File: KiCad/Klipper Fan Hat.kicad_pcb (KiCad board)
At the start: 2 copper layers, 65 x 56 mm, 62 parts, among them J1 Vin, J2 Serial, J3 I2C, J4 1 Wire, J5 GPIO5, J6 GPIO6, J7 SPI, J8 GPIO, Q1 IRLML6344, Q2 IRLML6344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

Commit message: update values of pull up resistors
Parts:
- R4, R5, R6: value 3.9k -> 4.7k

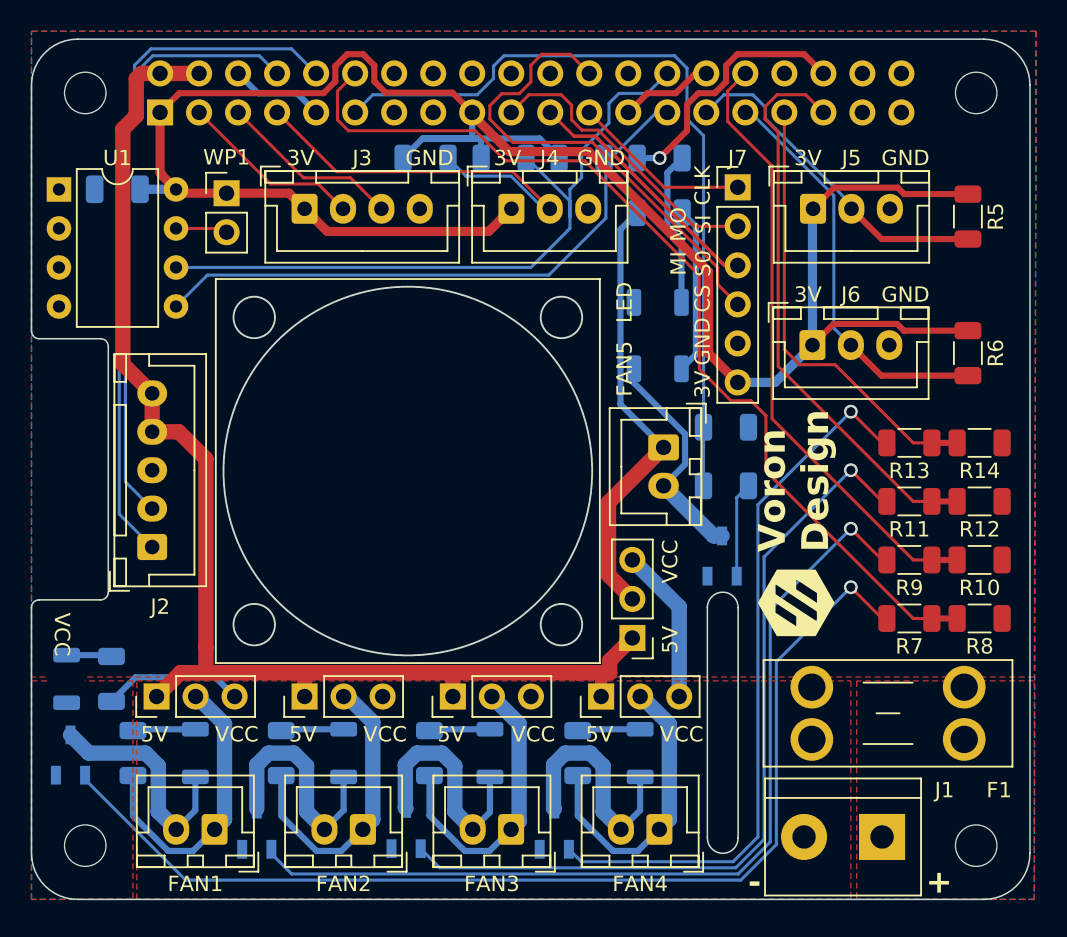
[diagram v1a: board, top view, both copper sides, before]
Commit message: Update KlippUpdate Klipper Fan Hat to expose more GPIO pins and add an on board DS18B20 Temperature Sensor
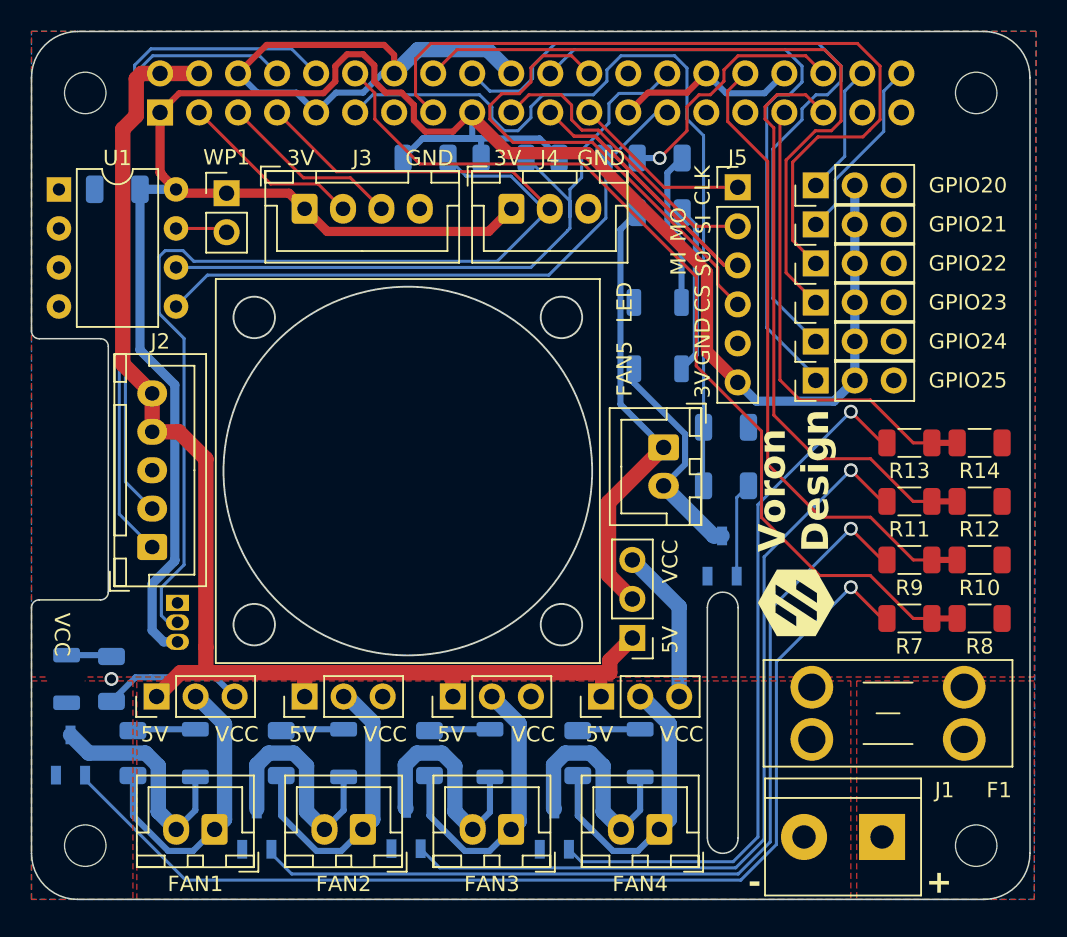
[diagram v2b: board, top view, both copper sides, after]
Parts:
- removed the J5 at (150.9, 55.0)
- removed R5, R6: 4.7k, Resistor_SMD:R_1206_3216Metric
- added GPIO20: J7, Connector_PinHeader_2.54mm:PinHeader_1x03_P2.54mm_Vertical, F.Cu at (151.1, 53.5)
- added GPIO21: J8, Connector_PinHeader_2.54mm:PinHeader_1x03_P2.54mm_Vertical, F.Cu at (151.1, 56.1)
- added GPIO22: J9, Connector_PinHeader_2.54mm:PinHeader_1x03_P2.54mm_Vertical, F.Cu at (151.1, 58.6)
- added GPIO24: J11, Connector_PinHeader_2.54mm:PinHeader_1x03_P2.54mm_Vertical, F.Cu at (151.1, 63.7)
- added GPIO25: J12, Connector_PinHeader_2.54mm:PinHeader_1x03_P2.54mm_Vertical, F.Cu at (151.1, 66.2)
- added U2: DS18B20, Package_TO_SOT_THT:TO-92_Inline, B.Cu at (109.5, 80.7)
- GPIO23: renamed from J6; value GPIO6 -> J10; footprint Connector_JST:JST_XH_B3B-XH-A_1x03_P2.50mm_Vertical -> Connector_PinHeader_2.54mm:PinHeader_1x03_P2.54mm_Vertical
- moved GPIO23 2.79 mm to (151.1, 61.1), turned to 90 degrees
- renumbered J7 to J5, J8 to J6
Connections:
- GPIO23 pad 1: +3V3 -> /GPIO23
- GPIO23 pad 2: /GPIO6 -> +3V3
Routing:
- net /GPIO4/GPCLK0: track 28.3 -> 81.5 mm
- net /GPIO22: track 0.00 -> 52.8 mm
- net /GPIO24: track 0.00 -> 48.2 mm
- net /GPIO23: track 0.00 -> 45.9 mm
- net /GPIO25: track 0.00 -> 40.7 mm
- net GND: track 12.3 -> 45.9 mm, vias 0 -> 1
- net /GPIO6: track 26.6 -> 0.00 mm
- net /GPIO5: track 22.0 -> 0.00 mm
- net +3V3: track 138.2 -> 157.1 mm
- net /GPIO21/PCM.DOUT: track 0.00 -> 12.1 mm
- net /GPIO20/PCM.DIN: track 0.00 -> 8.55 mm
- net /GPIO17: track 51.6 -> 54.3 mm
- net /GPIO19/PCM.FS: track 37.1 -> 39.2 mm
- net /GPIO12/PWM0: track 40.0 -> 41.9 mm
- net /GPIO13/PWM1: track 29.2 -> 30.8 mm
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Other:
- board size 65 x 56 mm -> 65 x 56.5 mm
- board text removed: "Extend PCB edge 0.5mm if using SMT header"

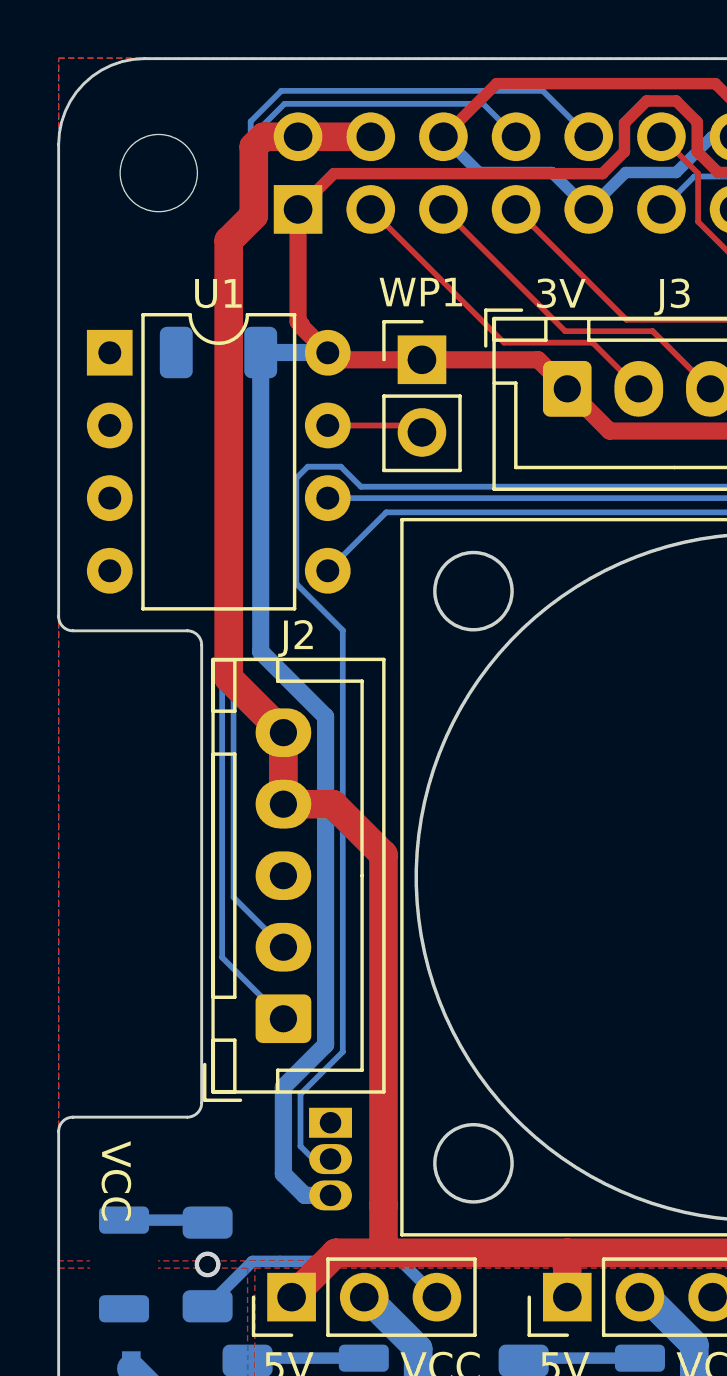
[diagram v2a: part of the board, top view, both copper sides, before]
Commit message: Update Serial Header Ground connection
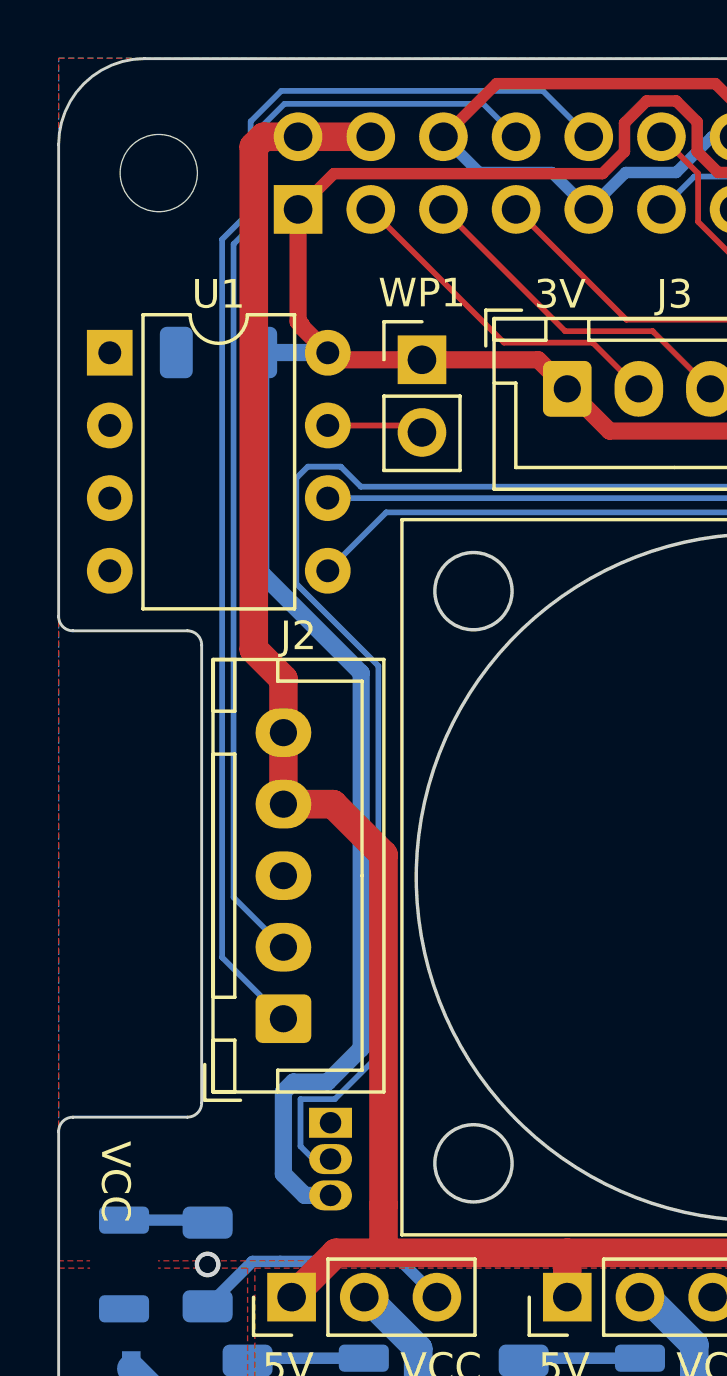
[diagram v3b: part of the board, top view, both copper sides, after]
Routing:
- net +3V3: track 157.1 -> 158.8 mm
- net /GPIO4/GPCLK0: track 81.5 -> 83.3 mm
- net +5V: track 84.2 -> 83.5 mm
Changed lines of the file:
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@@
   (segment (start 119.846 52.626) (end 131.326 52.626) (width 0.2) (layer "F.Cu") (net 4))
   (segment (start 128.2915 52.915) (end 127.1165 51.74) (width 0.2) (layer "B.Cu") (net 4))
+  (segment (start 130.322 58.462) (end 133.742 55.042) (width 0.2) (layer "B.Cu") (net 4))
+  (segment (start 133.742 55.042) (end 133.344817 55.042) (width 0.2) (layer "B.Cu") (net 4))
+  (segment (start 108.454 79.871) (end 109.652 79.871) (width 0.2) (layer "B.Cu") (net 4))
+  (segment (start 131.217817 52.915) (end 128.2915 52.915) (width 0.2) (layer "B.Cu") (net 4))
+  (segment (start 108.308 61.857635) (end 108.308 58.164) (width 0.2) (layer "B.Cu") (net 4))
+  (segment (start 108.308 58.164) (end 108.71 57.762) (width 0.2) (layer "B.Cu") (net 4))
+  (segment (start 110.563635 58.462) (end 130.322 58.462) (width 0.2) (layer "B.Cu") (net 4))
+  (segment (start 111.176 78.347) (end 111.176 64.725636) (width 0.2) (layer "B.Cu") (net 4))
+  (segment (start 108.454 81.521) (end 108.454 79.871) (width 0.2) (layer "B.Cu") (net 4))
   (segment (start 108.71 57.762) (end 109.863635 57.762) (width 0.2) (layer "B.Cu") (net 4))
-  (segment (start 133.742 55.042) (end 133.344817 55.042) (width 0.2) (layer "B.Cu") (net 4))
-  (segment (start 108.454 81.521) (end 108.454 79.697188) (width 0.2) (layer "B.Cu") (net 4))
-  (segment (start 108.308 61.857635) (end 108.308 58.164) (width 0.2) (layer "B.Cu") (net 4))
+  (segment (start 133.344817 55.042) (end 131.217817 52.915) (width 0.2) (layer "B.Cu") (net 4))
+  (segment (start 109.652 79.871) (end 111.176 78.347) (width 0.2) (layer "B.Cu") (net 4))
+  (segment (start 109.504 81.966) (end 108.899 81.966) (width 0.2) (layer "B.Cu") (net 4))
+  (segment (start 111.176 64.725636) (end 108.308 61.857635) (width 0.2) (layer "B.Cu") (net 4))
+  (segment (start 108.899 81.966) (end 108.454 81.521) (width 0.2) (layer "B.Cu") (net 4))
   (segment (start 109.863635 57.762) (end 110.563635 58.462) (width 0.2) (layer "B.Cu") (net 4))
-  (segment (start 108.454 79.697188) (end 109.932 78.219188) (width 0.2) (layer "B.Cu") (net 4))
-  (segment (start 131.217817 52.915) (end 128.2915 52.915) (width 0.2) (layer "B.Cu") (net 4))
-  (segment (start 109.932 63.481635) (end 108.308 61.857635) (width 0.2) (layer "B.Cu") (net 4))
-  (segment (start 110.563635 58.462) (end 130.322 58.462) (width 0.2) (layer "B.Cu") (net 4))
-  (segment (start 108.899 81.966) (end 108.454 81.521) (width 0.2) (layer "B.Cu") (net 4))
-  (segment (start 109.504 81.966) (end 108.899 81.966) (width 0.2) (layer "B.Cu") (net 4))
-  (segment (start 130.322 58.462) (end 133.742 55.042) (width 0.2) (layer "B.Cu") (net 4))
-  (segment (start 133.344817 55.042) (end 131.217817 52.915) (width 0.2) (layer "B.Cu") (net 4))
-  (segment (start 109.932 78.219188) (end 109.932 63.481635) (width 0.2) (layer "B.Cu") (net 4))
-  (segment (start 108.308 58.164) (end 108.71 57.762) (width 0.2) (layer "B.Cu") (net 4))
   (segment (start 107.893654 45.08) (end 114.84 45.08) (width 0.2) (layer "B.Cu") (net 5))
   (segment (start 106.115 49.981686) (end 107.112 48.984686) (width 0.2) (layer "B.Cu") (net 5))
@@
   (segment (start 155.48 50.005654) (end 152.324 53.161654) (width 0.2) (layer "B.Cu") (net 29))
   (segment (start 156.63 46.23) (end 155.48 47.38) (width 0.2) (layer "B.Cu") (net 29))
+  (segment (start 107.167919 46.23) (end 106.82 46.577919) (width 1) (layer "F.Cu") (net 30))
+  (segment (start 108.37 46.23) (end 107.167919 46.23) (width 1) (layer "F.Cu") (net 30))
   (segment (start 111.3538 85.242) (end 117.78 85.242) (width 1) (layer "F.Cu") (net 30))
   (segment (start 111.3538 83.5812) (end 111.3538 85.242) (width 1) (layer "F.Cu") (net 30))
-  (segment (start 107.8524 67.06) (end 105.9436 65.1512) (width 1) (layer "F.Cu") (net 30))
   (segment (start 127.432 85.242) (end 135.534 85.242) (width 1) (layer "F.Cu") (net 30))
-  (segment (start 106.82 48.984) (end 106.82 46.577919) (width 1) (layer "F.Cu") (net 30))
   (segment (start 137.6428 84.4552) (end 139.116 82.982) (width 1) (layer "F.Cu") (net 30))
   (segment (start 137.6428 85.2426) (end 137.6428 84.4552) (width 1) (layer "F.Cu") (net 30))
   (segment (start 107.857 69.56) (end 107.857 67.06) (width 1) (layer "F.Cu") (net 30))
   (segment (start 111.3538 71.3234) (end 111.3538 83.5812) (width 1) (layer "F.Cu") (net 30))
-  (segment (start 107.167919 46.23) (end 108.37 46.23) (width 1) (layer "F.Cu") (net 30))
   (segment (start 109.693 85.242) (end 108.143 86.792) (width 1) (layer "F.Cu") (net 30))
   (segment (start 135.534 85.242) (end 135.5346 85.2426) (width 1) (layer "F.Cu") (net 30))
   (segment (start 107.857 69.56) (end 109.5904 69.56) (width 1) (layer "F.Cu") (net 30))
   (segment (start 111.3538 85.242) (end 109.693 85.242) (width 1) (layer "F.Cu") (net 30))
+  (segment (start 106.82 64.148) (end 107.857 65.185) (width 1) (layer "F.Cu") (net 30))
   (segment (start 135.5346 85.2426) (end 137.084 85.2426) (width 1) (layer "F.Cu") (net 30))
-  (segment (start 105.9436 65.1512) (end 105.9436 49.8604) (width 1) (layer "F.Cu") (net 30))
-  (segment (start 107.857 67.06) (end 107.8524 67.06) (width 1) (layer "F.Cu") (net 30))
-  (segment (start 106.82 46.577919) (end 107.167919 46.23) (width 1) (layer "F.Cu") (net 30))
+  (segment (start 107.857 65.185) (end 107.857 67.06) (width 1) (layer "F.Cu") (net 30))
   (segment (start 127.432 86.792) (end 127.432 85.242) (width 1) (layer "F.Cu") (net 30))
   (segment (start 137.084 86.792) (end 137.084 85.2426) (width 0.8) (layer "F.Cu") (net 30))
+  (segment (start 106.82 46.577919) (end 106.82 64.148) (width 1) (layer "F.Cu") (net 30))
   (segment (start 109.5904 69.56) (end 111.3538 71.3234) (width 1) (layer "F.Cu") (net 30))
   (segment (start 117.78 86.792) (end 117.78 85.242) (width 1) (layer "F.Cu") (net 30))
@@
   (segment (start 137.084 85.2426) (end 137.6428 85.2426) (width 1) (layer "F.Cu") (net 30))
   (segment (start 117.78 85.242) (end 127.432 85.242) (width 1) (layer "F.Cu") (net 30))
-  (segment (start 105.9436 49.8604) (end 106.82 48.984) (width 1) (layer "F.Cu") (net 30))
   (segment (start 128.69 49.052844) (end 128.69 48.77) (width 0.8) (layer "F.Cu") (net 31))
   (segment (start 108.37 52.6932) (end 108.37 48.77) (width 0.6) (layer "F.Cu") (net 31))
@@
   (segment (start 108.4836 52.8576) (end 108.4836 52.8068) (width 0.6) (layer "F.Cu") (net 31))
   (segment (start 107.063 53.772) (end 109.398 53.772) (width 0.6) (layer "B.Cu") (net 31))
+  (segment (start 107.854 79.622472) (end 108.205472 79.271) (width 0.6) (layer "B.Cu") (net 31))
   (segment (start 153.594 56.058) (end 153.594 53.518) (width 0.6) (layer "B.Cu") (net 31))
-  (segment (start 107.854 79.44866) (end 107.854 82.486) (width 0.6) (layer "B.Cu") (net 31))
   (segment (start 153.594 58.598) (end 153.594 56.058) (width 0.6) (layer "B.Cu") (net 31))
-  (segment (start 107.854 82.486) (end 108.604 83.236) (width 0.6) (layer "B.Cu") (net 31))
+  (segment (start 110.576 78.098472) (end 110.576 64.974163) (width 0.6) (layer "B.Cu") (net 31))
   (segment (start 128.69 48.77) (end 128.69 50.453) (width 0.4) (layer "B.Cu") (net 31))
+  (segment (start 110.576 64.974163) (end 107.063 61.461163) (width 0.6) (layer "B.Cu") (net 31))
   (segment (start 152.244 67.568) (end 147.197 67.568) (width 0.6) (layer "B.Cu") (net 31))
   (segment (start 125.4665 50.465) (end 124.1915 51.74) (width 0.4) (layer "B.Cu") (net 31))
-  (segment (start 107.063 53.772) (end 107.063 64.231812) (width 0.6) (layer "B.Cu") (net 31))
+  (segment (start 108.604 83.236) (end 107.854 82.486) (width 0.6) (layer "B.Cu") (net 31))
   (segment (start 133.0765 50.465) (end 125.4665 50.465) (width 0.4) (layer "B.Cu") (net 31))
   (segment (start 153.594 66.218) (end 152.244 67.568) (width 0.6) (layer "B.Cu") (net 31))
-  (segment (start 108.604 83.236) (end 109.504 83.236) (width 0.6) (layer "B.Cu") (net 31))
+  (segment (start 107.063 61.461163) (end 107.063 53.772) (width 0.6) (layer "B.Cu") (net 31))
   (segment (start 133.0765 50.465) (end 134.3515 51.74) (width 0.4) (layer "B.Cu") (net 31))
+  (segment (start 109.504 83.236) (end 108.604 83.236) (width 0.6) (layer "B.Cu") (net 31))
   (segment (start 109.398 53.772) (end 109.408 53.782) (width 0.6) (layer "B.Cu") (net 31))
-  (segment (start 107.063 64.231812) (end 109.332 66.500812) (width 0.6) (layer "B.Cu") (net 31))
   (segment (start 153.594 63.678) (end 153.594 61.138) (width 0.6) (layer "B.Cu") (net 31))
   (segment (start 129.2715 51.74) (end 129.2715 50.5265) (width 0.4) (layer "B.Cu") (net 31))
   (segment (start 147.197 67.568) (end 145.974 66.345) (width 0.6) (layer "B.Cu") (net 31))
+  (segment (start 109.403472 79.271) (end 110.576 78.098472) (width 0.6) (layer "B.Cu") (net 31))
+  (segment (start 107.854 82.486) (end 107.854 79.622472) (width 0.6) (layer "B.Cu") (net 31))
   (segment (start 153.594 61.138) (end 153.594 58.598) (width 0.6) (layer "B.Cu") (net 31))
   (segment (start 128.702 50.465) (end 125.4665 50.465) (width 0.4) (layer "B.Cu") (net 31))
   (segment (start 128.69 50.453) (end 128.702 50.465) (width 0.4) (layer "B.Cu") (net 31))
-  (segment (start 109.332 77.97066) (end 107.854 79.44866) (width 0.6) (layer "B.Cu") (net 31))
   (segment (start 128.702 50.465) (end 129.21 50.465) (width 0.4) (layer "B.Cu") (net 31))
-  (segment (start 109.332 66.500812) (end 109.332 77.881472) (width 0.6) (layer "B.Cu") (net 31))
+  (segment (start 108.205472 79.271) (end 109.403472 79.271) (width 0.6) (layer "B.Cu") (net 31))
   (segment (start 129.2715 50.5265) (end 129.21 50.465) (width 0.4) (layer "B.Cu") (net 31))
-  (segment (start 109.332 77.881472) (end 109.332 77.97066) (width 0.6) (layer "B.Cu") (net 31))
   (segment (start 153.594 66.218) (end 153.594 63.678) (width 0.6) (layer "B.Cu") (net 31))
   (segment (start 139.116 80.442) (end 137.566 78.892) (width 1) (layer "F.Cu") (net 35))
